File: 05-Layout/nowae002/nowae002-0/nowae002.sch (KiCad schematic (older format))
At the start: 56 parts, among them J1 SMALL_JUMPER, J2 SMALL_JUMPER, J3 SMALL_JUMPER, P1 USB_A_90, Q1 IRLML6402, U1 FT230XQ, U2 TPS62152, U3 RN4870

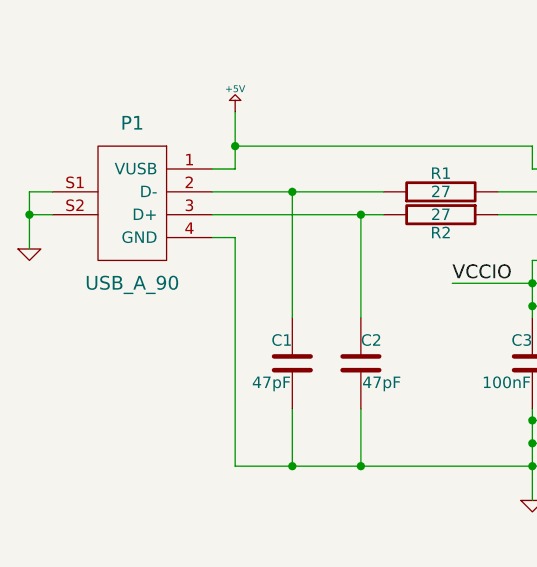
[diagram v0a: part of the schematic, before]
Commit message: Changed P1 footprint and updated net file (nowae002-0)
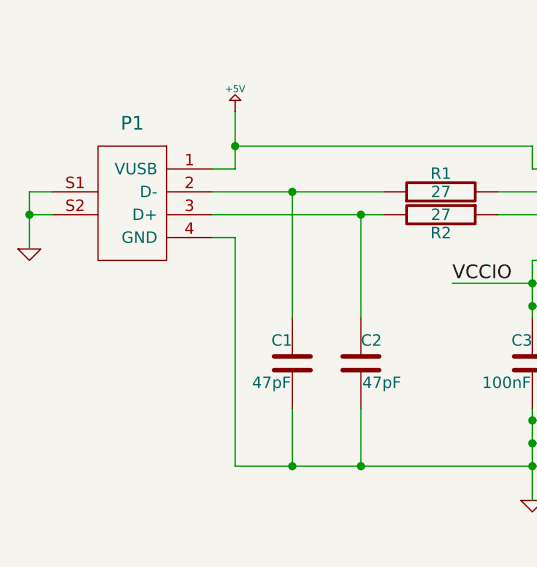
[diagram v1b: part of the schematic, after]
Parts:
- P1: footprint CONNECTOR:USB-A-PLUG-SMD -> CONNECTOR:USB-A-WURTH-629004113921
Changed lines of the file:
@@
 EESchema Schematic File Version 2
-LIBS:nowae002-rescue
 LIBS:nowae-analog
 LIBS:nowae-batterycharger
@@
 P 4300 2300
 F 0 "P1" H 4300 2650 60  0000 C CNN
-F 1 "USB_A_90" H 4300 1950 60  0000 C CNN
-F 2 "CONNECTOR:USB-A-PLUG-SMD" H 4675 2300 60  0001 C CNN
+F 1 "USB_A_90" H 4300 1950 60  0001 C CNN
+F 2 "CONNECTOR:USB-A-WURTH-629004113921" H 4675 2300 60  0001 C CNN
 F 3 "" H 4675 2300 60  0000 C CNN
 F 4 "Molex" H 4300 1850 60  0001 C CNN "Manufacturer"

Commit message: Updated P1 informations (nowae002-0)
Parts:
- P1: Distributor RS Components -> Farnell Italia S.r.l.; Distributor Code 800-6772 -> 2442732; Manufacturer Molex -> Wurth Elektronik; Part Number 48037-2200 -> 629004113921; Price € 1.47 -> 2.88
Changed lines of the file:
@@
 F 2 "CONNECTOR:USB-A-WURTH-629004113921" H 4675 2300 60  0001 C CNN
 F 3 "" H 4675 2300 60  0000 C CNN
-F 4 "Molex" H 4300 1850 60  0001 C CNN "Manufacturer"
-F 5 "48037-2200" H 4300 1750 60  0001 C CNN "Part Number"
-F 6 "RS Components" H 4300 1650 60  0001 C CNN "Distributor"
-F 7 "800-6772" H 4300 1550 60  0001 C CNN "Distributor Code"
-F 8 "1.47" H 4300 1450 60  0001 C CNN "Price €"
+F 4 "Wurth Elektronik" H 4300 1850 60  0001 C CNN "Manufacturer"
+F 5 "629004113921" H 4300 1750 60  0001 C CNN "Part Number"
+F 6 "Farnell Italia S.r.l." H 4300 1650 60  0001 C CNN "Distributor"
+F 7 "2442732" H 4300 1550 60  0001 C CNN "Distributor Code"
+F 8 "2.88" H 4300 1450 60  0001 C CNN "Price €"
 	1    4300 2300
 	1    0    0    -1

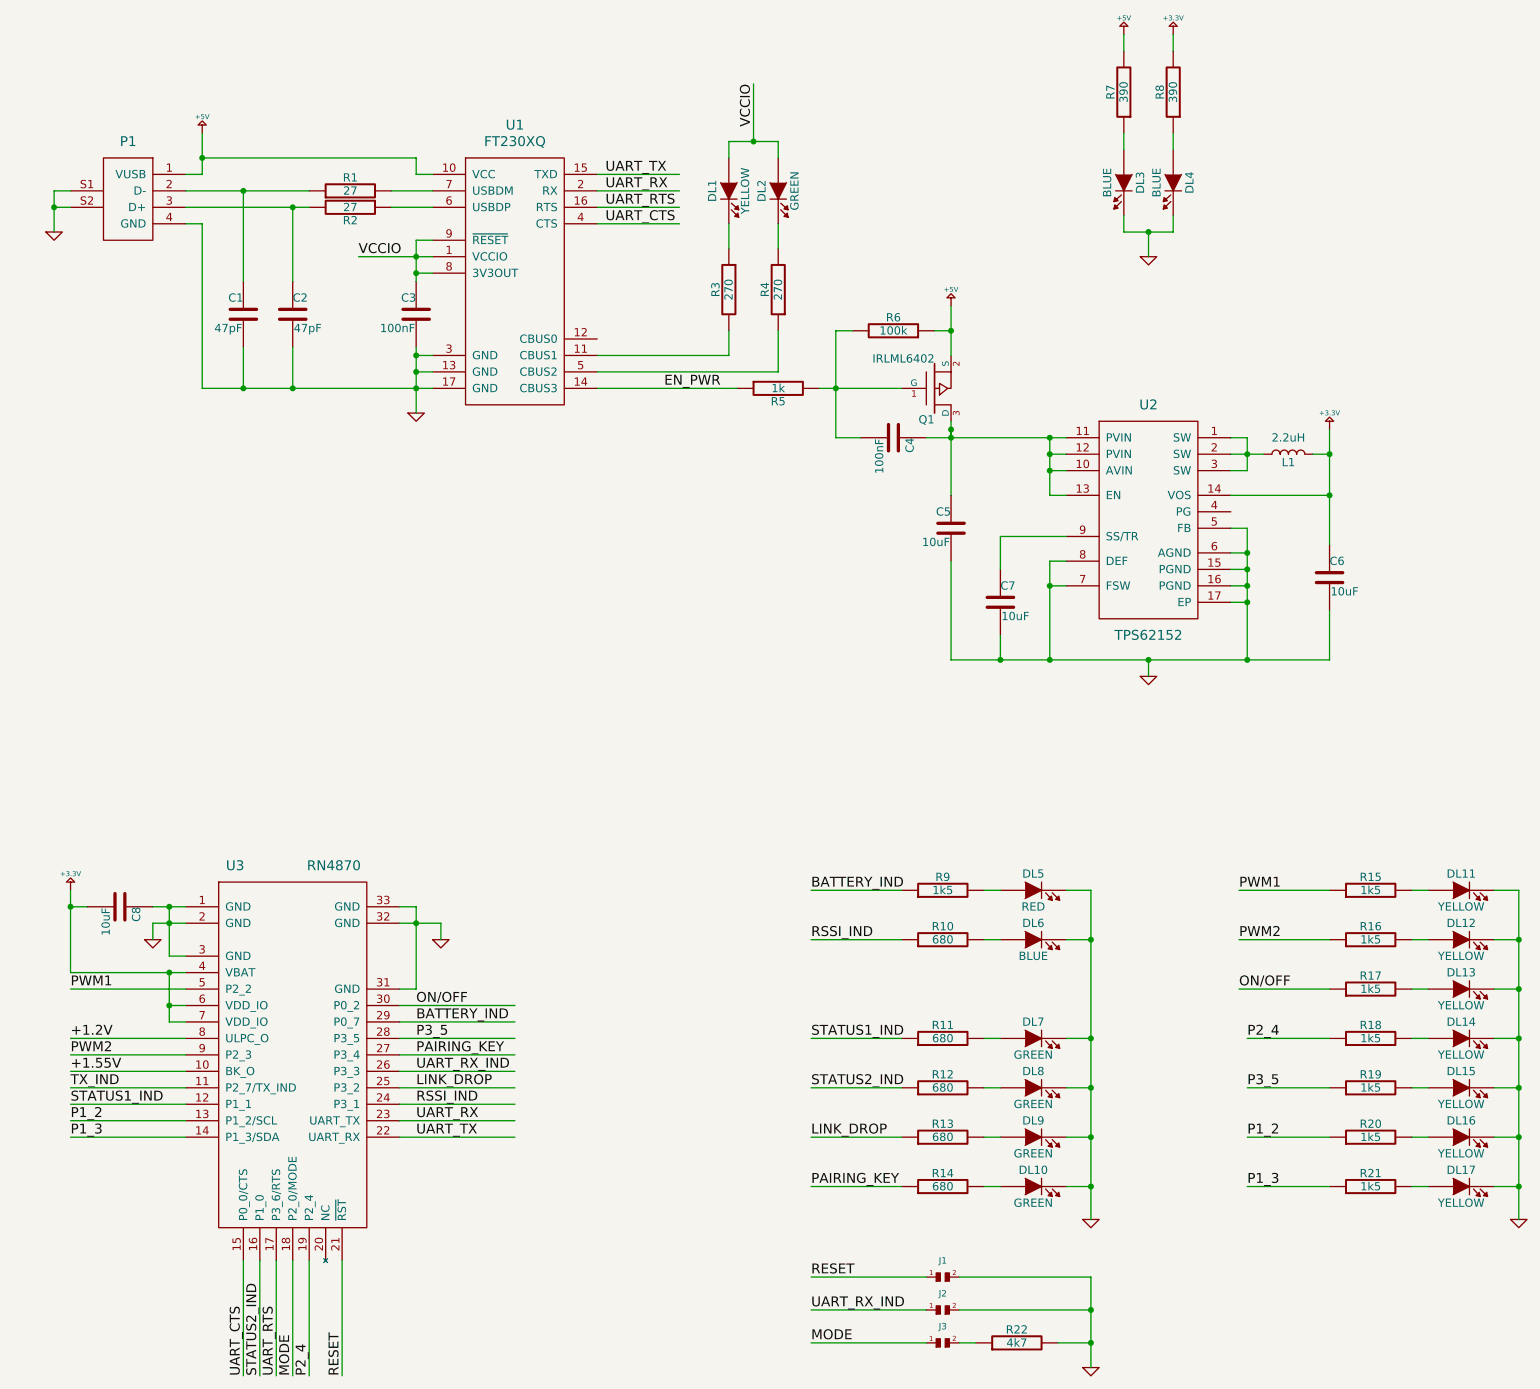
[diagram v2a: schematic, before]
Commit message: Changed CBUS pins (nowae002-0) Minor fix (nowae002-0)
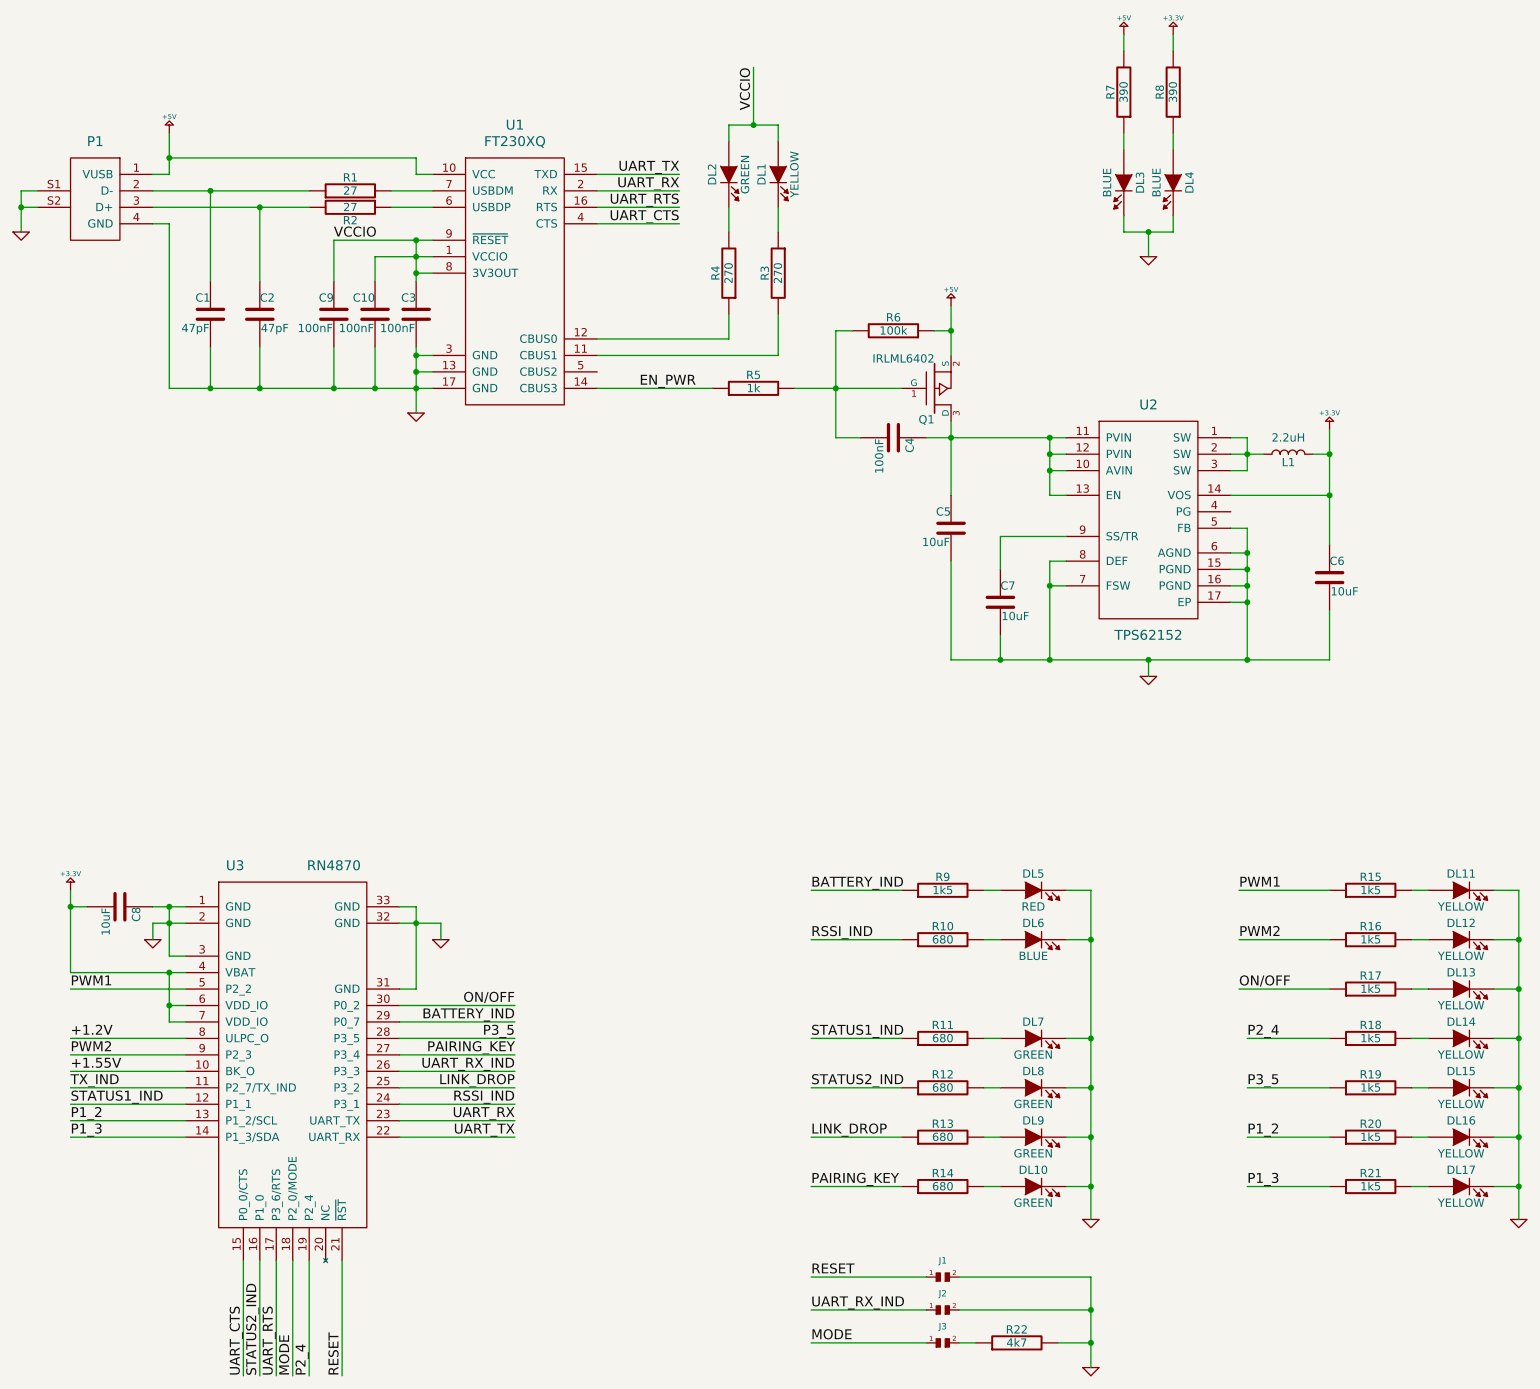
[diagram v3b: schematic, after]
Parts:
- added C10, C9: 100nF, CAPACITOR:CAPACITOR-0402, symbol CAPACITOR
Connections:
- wire segments 173 -> 236
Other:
- moved on the sheet: C1, C2, DL1, DL2, P1, R3, R4, R5
